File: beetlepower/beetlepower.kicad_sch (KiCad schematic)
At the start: 14 parts, among them J1 Battery, J2 OUT2, J3 OUT3, J4 OUT4, J5 Conn_01x03_Male, U1 L7805

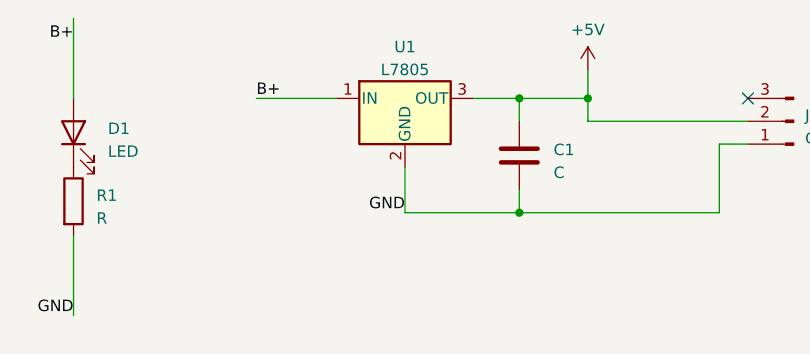
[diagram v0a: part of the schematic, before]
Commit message: PCBs for send off
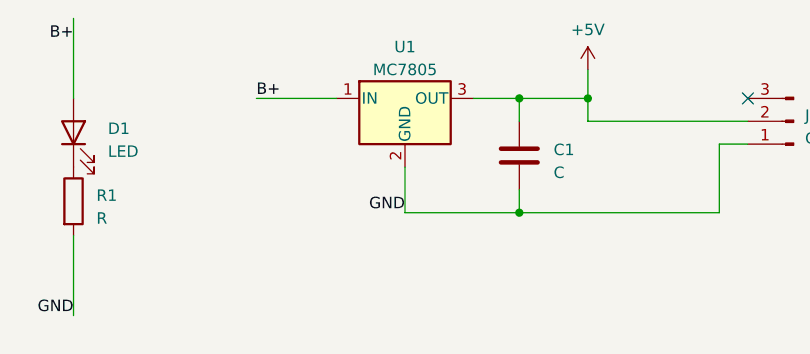
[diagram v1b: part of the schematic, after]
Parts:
- U1: value L7805 -> MC7805; footprint Package_TO_SOT_THT:TO-220-3_Vertical -> Package_TO_SOT_SMD:TO-252-3_TabPin2
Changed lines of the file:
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@@
     (in_bom yes) (on_board yes) (fields_autoplaced)
     (property "Reference" "U1" (id 0) (at 173.99 64.77 0))
-    (property "Value" "L7805" (id 1) (at 173.99 67.31 0))
-    (property "Footprint" "Package_TO_SOT_THT:TO-220-3_Vertical" (id 2) (at 174.625 74.295 0)
+    (property "Value" "MC7805" (id 1) (at 173.99 67.31 0))
+    (property "Footprint" "Package_TO_SOT_SMD:TO-252-3_TabPin2" (id 2) (at 174.625 74.295 0)
       (effects (font (size 1.27 1.27) italic) (justify left) hide)
     )
@@
     )
     (path "/c3c1864a-2ff6-40d5-b620-ea0426ce4ee0"
-      (reference "U1") (unit 1) (value "L7805") (footprint "Package_TO_SOT_THT:TO-220-3_Vertical")
+      (reference "U1") (unit 1) (value "MC7805") (footprint "Package_TO_SOT_SMD:TO-252-3_TabPin2")
     )
   )

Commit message: special footprints for pth+smd
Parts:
- C1: footprint Capacitor_THT:C_Disc_D7.0mm_W2.5mm_P5.00mm -> beetlepower-xt30:C-pth-and-smd
- R1: footprint Resistor_THT:R_Axial_DIN0207_L6.3mm_D2.5mm_P10.16mm_Horizontal -> beetlepower-xt30:Resistor-pth-and-smd
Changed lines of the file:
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@@
       (effects (font (size 1.27 1.27)) (justify left))
     )
-    (property "Footprint" "Resistor_THT:R_Axial_DIN0207_L6.3mm_D2.5mm_P10.16mm_Horizontal" (id 2) (at 135.382 81.915 90)
+    (property "Footprint" "beetlepower-xt30:Resistor-pth-and-smd" (id 2) (at 135.382 81.915 90)
       (effects (font (size 1.27 1.27)) hide)
     )
@@
       (effects (font (size 1.27 1.27)) (justify left))
     )
-    (property "Footprint" "Capacitor_THT:C_Disc_D7.0mm_W2.5mm_P5.00mm" (id 2) (at 187.6552 80.645 0)
+    (property "Footprint" "beetlepower-xt30:C-pth-and-smd" (id 2) (at 187.6552 80.645 0)
       (effects (font (size 1.27 1.27)) hide)
     )
@@
     )
     (path "/e185f8e6-3657-4e72-8333-bee9105cbce1"
-      (reference "C1") (unit 1) (value "C") (footprint "Capacitor_THT:C_Disc_D7.0mm_W2.5mm_P5.00mm")
+      (reference "C1") (unit 1) (value "C") (footprint "beetlepower-xt30:C-pth-and-smd")
     )
     (path "/bb80ddbd-1c56-4016-90b2-e3035e5a6227"
@@
     )
     (path "/41ea4b02-622d-4689-9b91-59bb0aaceccc"
-      (reference "R1") (unit 1) (value "R") (footprint "Resistor_THT:R_Axial_DIN0207_L6.3mm_D2.5mm_P10.16mm_Horizontal")
+      (reference "R1") (unit 1) (value "R") (footprint "beetlepower-xt30:Resistor-pth-and-smd")
     )
     (path "/c3c1864a-2ff6-40d5-b620-ea0426ce4ee0"
